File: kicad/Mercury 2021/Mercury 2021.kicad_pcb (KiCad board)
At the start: 2 copper layers, 57 parts, among them J1 Batt_Power, J10 3.3v rail, J11 Screw_Terminal_01x02, J12 Screw_Terminal_01x02, J13 Screw_Terminal_01x02, J14 Screw_Terminal_01x02, J15 Raspberry_Pi_2_3, J16 Sensors_Extra, J17 Arduino_Extra_Power, J18 Arduino_Extra_Comm, J19 Arduino_Extra_Digital, J2 Screw_Terminal_01x02, J20 Arduino_Extra_Analog, J21 MP_Extra_Analog, J22 Servos_Connector, J23 Pi_Extra_Comm, J24 Pi_Extra_GPIO, J25 Pi_Extra_GPIO, J26 Pi_Extra_Power, J27 Pi_Extra_GND, J28 Pi_Extra_GPIO, J29 Pi_Extra_GPIO, J3 Screw_Terminal_01x02, J30 Screw_Terminal_01x02, J31 Screw_Terminal_01x02, J32 Screw_Terminal_01x02, J33 Screw_Terminal_01x02, J34 Screw_Terminal_01x02, J35 Screw_Terminal_01x02, J36 GND rail 2, J37 GND rail 3, J38 USB_B, J39 USB_A, J4 Screw_Terminal_01x02, J5 Screw_Terminal_01x02, J6 Screw_Terminal_01x02, J7 5V rail, J8 GND Rail 1, J9 11v rail, U1 LM1084-5.0, U10 TCA9548APWR, U11 PCA9685, U12 PCA9685, U13 PCA9685, U2 Adafruit_VL53L0X, U3 Adafruit_VL53L0X, U4 Adafruit_VL53L0X, U5 Adafruit_VL53L0X, U6 Adafruit_VL53L0X, U7 Adafruit_VL53L0X, U8 Adafruit_VL53L0X, U9 Adafruit_VL53L0X

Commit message: Updated new board
- Did PCB traces
-- almost got away with just 2 copper layers, pi ruined it when there was only a bit to go. Probably possible but would take a lot of back and forth
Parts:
- removed C4: 10μf, Capacitor_THT:CP_Radial_D10.0mm_P2.50mm
- added U12A1: PCA9685, Connector_PinSocket_2.54mm:PinSocket_1x03_P2.54mm_Vertical, F.Cu at (83.6, 36.4)
- added U12B1: PCA9685, Connector_PinSocket_2.54mm:PinSocket_1x03_P2.54mm_Vertical, F.Cu at (80.0, 36.4)
- added U12C1: PCA9685, TerminalBlock:TerminalBlock_Altech_AK300-2_P5.00mm, F.Cu at (63.4, 87.9)
- added U12D1: PCA9685, Connector_PinSocket_2.54mm:PinSocket_1x03_P2.54mm_Vertical, F.Cu at (87.1, 36.4)
- added U12E1: PCA9685, Connector_PinSocket_2.54mm:PinSocket_1x03_P2.54mm_Vertical, F.Cu at (90.7, 36.4)
- J22: footprint Connector_PinSocket_2.54mm:PinSocket_2x03_P2.54mm_Vertical -> Connector_PinHeader_2.54mm:PinHeader_2x03_P2.54mm_Vertical
- U11, U13: footprint Connector_PinHeader_2.54mm:PinHeader_1x05_P2.54mm_Vertical -> Connector_JST:JST_EH_B5B-EH-A_1x05_P2.50mm_Vertical
- U12: footprint Connector_PinHeader_2.54mm:PinHeader_1x06_P2.54mm_Vertical -> Connector_PinSocket_2.54mm:PinSocket_1x06_P2.54mm_Vertical
- moved J8 248.1 mm to (48.4, 162.5)
- moved J7 246.5 mm to (48.5, 167.5)
- moved J9 231.0 mm to (37.5, 122.3), turned to 0 degrees
- moved J13 230.9 mm to (19.5, 112.1), turned to 90 degrees
- moved J34 221.2 mm to (19.2, 129.1), turned to 90 degrees
- moved J36 218.7 mm to (42.5, 122.5), turned to 0 degrees
- moved J11 213.4 mm to (19.5, 145.3), turned to 90 degrees
- moved J30 207.5 mm to (19.7, 163.1), turned to 90 degrees
- moved J32 206.0 mm to (18.9, 179.9), turned to 90 degrees
- moved J12 198.8 mm to (117.9, 182.9)
- moved J14 198.8 mm to (84.1, 182.9)
- moved J31 198.8 mm to (100.9, 182.9)
- moved J33 198.8 mm to (50.1, 182.9)
- moved J35 198.8 mm to (66.9, 182.9)
- moved C2 182.2 mm to (36.9, 162.1)
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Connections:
- net Arduino_3v3 renamed 3.3v_Rail
- net LM_VIN renamed 11.1v_Rail
- net SUB_D- renamed USB_D-
- C1 pad 2: LM_GND_MAIN -> GND_Rail
- C2 pad 1: MP_5v -> 5v_Rail
- C2 pad 2: LM_GND_MAIN -> GND_Rail
- C3 pad 2: Net-(C3-Pad2) -> GND_Rail
- J1 pad 1: LM_GND_MAIN -> GND_Rail
- J11 pad 1: LM_GND_MAIN -> GND_Rail
- J12 pad 1: MP_5v -> 5v_Rail
- J12 pad 2: LM_GND_MAIN -> GND_Rail
- J13 pad 1: LM_GND_MAIN -> GND_Rail
- J14 pad 1: MP_5v -> 5v_Rail
- J14 pad 2: LM_GND_MAIN -> GND_Rail
- J15 pad 1: /Motors/Pi_3v3 -> /Motors/Pi_3v3a
- J15 pad 17: /Motors/Pi_3v3 -> /Motors/Pi_3v3b
- J15 pad 2: MP_5v -> 5v_Rail
- J15 pad 20: LM_GND_MAIN -> /Motors/Pi_GNDa
- J15 pad 25: LM_GND_MAIN -> /Motors/Pi_GNDb
- J15 pad 30: LM_GND_MAIN -> /Motors/Pi_GNDc
- J15 pad 34: LM_GND_MAIN -> /Motors/Pi_GNDe
- J15 pad 39: Net-(J15-Pad39) -> GND_Rail
- J15 pad 4: MP_5v -> /Motors/Pi_5v_a
- J2 pad 2: LM_GND_MAIN -> GND_Rail
- J26 pad 1: MP_5v -> Net-(J26-Pad1)
- J26 pad 2: MP_5v -> /Motors/Pi_5v_a
- J26 pad 4: /Motors/Pi_3v3 -> /Motors/Pi_3v3a
- J26 pad 5: /Motors/Pi_3v3 -> /Motors/Pi_3v3b
- J27 pad 1: LM_GND_MAIN -> Net-(J27-Pad1)
- J27 pad 2: LM_GND_MAIN -> /Motors/Pi_GNDe
- J27 pad 3: LM_GND_MAIN -> /Motors/Pi_GNDc
- J27 pad 4: LM_GND_MAIN -> /Motors/Pi_GNDb
- J27 pad 5: LM_GND_MAIN -> /Motors/Pi_GNDa
- J3 pad 2: LM_GND_MAIN -> GND_Rail
- J30 pad 1: LM_GND_MAIN -> GND_Rail
- J31 pad 1: MP_5v -> 5v_Rail
- J31 pad 2: LM_GND_MAIN -> GND_Rail
- J32 pad 1: LM_GND_MAIN -> GND_Rail
- J33 pad 1: MP_5v -> 5v_Rail
- J33 pad 2: LM_GND_MAIN -> GND_Rail
- J34 pad 1: LM_GND_MAIN -> GND_Rail
- J35 pad 1: MP_5v -> 5v_Rail
- J35 pad 2: LM_GND_MAIN -> GND_Rail
- J36 pad 1: LM_GND_MAIN -> GND_Rail
- J36 pad 10: LM_GND_MAIN -> GND_Rail
- J36 pad 11: LM_GND_MAIN -> GND_Rail
- J36 pad 2: LM_GND_MAIN -> GND_Rail
- J36 pad 3: LM_GND_MAIN -> GND_Rail
- J36 pad 4: LM_GND_MAIN -> GND_Rail
- J36 pad 5: LM_GND_MAIN -> GND_Rail
- J36 pad 6: LM_GND_MAIN -> GND_Rail
- J36 pad 7: LM_GND_MAIN -> GND_Rail
- J36 pad 8: LM_GND_MAIN -> GND_Rail
- J36 pad 9: LM_GND_MAIN -> GND_Rail
- J37 pad 1: LM_GND_MAIN -> GND_Rail
- J37 pad 10: LM_GND_MAIN -> GND_Rail
- J37 pad 11: LM_GND_MAIN -> GND_Rail
- J37 pad 2: LM_GND_MAIN -> GND_Rail
- J37 pad 3: LM_GND_MAIN -> GND_Rail
- J37 pad 4: LM_GND_MAIN -> GND_Rail
- J37 pad 5: LM_GND_MAIN -> GND_Rail
- J37 pad 6: LM_GND_MAIN -> GND_Rail
- J37 pad 7: LM_GND_MAIN -> GND_Rail
- J37 pad 8: LM_GND_MAIN -> GND_Rail
- J37 pad 9: LM_GND_MAIN -> GND_Rail
- J4 pad 2: LM_GND_MAIN -> GND_Rail
- J5 pad 2: LM_GND_MAIN -> GND_Rail
- J6 pad 2: LM_GND_MAIN -> GND_Rail
- J7 pad 1: MP_5v -> 5v_Rail
- J7 pad 10: MP_5v -> 5v_Rail
- J7 pad 11: MP_5v -> 5v_Rail
- J7 pad 2: MP_5v -> 5v_Rail
- J7 pad 3: MP_5v -> 5v_Rail
- J7 pad 4: MP_5v -> 5v_Rail
- J7 pad 5: MP_5v -> 5v_Rail
- J7 pad 6: MP_5v -> 5v_Rail
- J7 pad 7: MP_5v -> 5v_Rail
- J7 pad 8: MP_5v -> 5v_Rail
- J7 pad 9: MP_5v -> 5v_Rail
- J8 pad 1: LM_GND_MAIN -> GND_Rail
- J8 pad 10: LM_GND_MAIN -> GND_Rail
- J8 pad 11: LM_GND_MAIN -> GND_Rail
- J8 pad 2: LM_GND_MAIN -> GND_Rail
- J8 pad 3: LM_GND_MAIN -> GND_Rail
- J8 pad 4: LM_GND_MAIN -> GND_Rail
- J8 pad 5: LM_GND_MAIN -> GND_Rail
- J8 pad 6: LM_GND_MAIN -> GND_Rail
- J8 pad 7: LM_GND_MAIN -> GND_Rail
- J8 pad 8: LM_GND_MAIN -> GND_Rail
- J8 pad 9: LM_GND_MAIN -> GND_Rail
- U1 pad 1: LM_GND_MAIN -> GND_Rail
- U1 pad 2: MP_5v -> 5v_Rail
- U10 pad 12: LM_GND_MAIN -> GND_Rail
- U10 pad 24: MP_5v -> 5v_Rail
- U12 pad 5: /Motors/Serco_VCC -> 5v_Rail
- U2 pad 1: MP_5v -> 5v_Rail
- U2 pad 2: LM_GND_MAIN -> GND_Rail
- U3 pad 1: MP_5v -> 5v_Rail
- U3 pad 2: LM_GND_MAIN -> GND_Rail
- U4 pad 1: MP_5v -> 5v_Rail
- U4 pad 2: LM_GND_MAIN -> GND_Rail
- U5 pad 1: MP_5v -> 5v_Rail
- U5 pad 2: LM_GND_MAIN -> GND_Rail
- U6 pad 1: MP_5v -> 5v_Rail
- U6 pad 2: LM_GND_MAIN -> GND_Rail
- U7 pad 1: MP_5v -> 5v_Rail
- U7 pad 2: LM_GND_MAIN -> GND_Rail
- U8 pad 1: /Sensors/VDD8 -> 5v_Rail
- U8 pad 2: /Sensors/GND8 -> GND_Rail
- U9 pad 1: MP_5v -> 5v_Rail
- U9 pad 2: LM_GND_MAIN -> GND_Rail
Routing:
- net GND_Rail: track 0.00 -> 995.7 mm, vias 0 -> 2
- net 5v_Rail: track 0.00 -> 683.0 mm
- net 3.3v_Rail: track 0.00 -> 286.9 mm
- net USB_GND: track 0.00 -> 269.0 mm
- net 11.1v_Rail: track 0.00 -> 164.5 mm
- net /Sensors/SDA: track 0.00 -> 153.1 mm
- net /Sensors/SCL: track 0.00 -> 126.1 mm
- net USB_D-: track 0.00 -> 126.1 mm
- net USB_D+: track 0.00 -> 125.5 mm
- net USB_VBUS: track 0.00 -> 123.9 mm
- net /Motors/RM_PWM2_GPIO12: track 0.00 -> 121.8 mm
- net USB_SHIELD: track 0.00 -> 121.5 mm
- net Net-(J22-Pad6): track 0.00 -> 97.8 mm, vias 0 -> 1
- net Net-(J22-Pad2): track 0.00 -> 97.4 mm, vias 0 -> 1
- net Net-(J22-Pad4): track 0.00 -> 97.1 mm, vias 0 -> 2
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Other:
- copper layers 2 -> 4
- board text added: "+"
- board text added: "-"
- board text added: "0"
- board text added: "00"
- board text added: "01"
- board text added: "04"
- board text added: "07"
- board text added: "08"
- board text added: "09"
- board text added: "1"
- board text added: "10"
- board text added: "11"
- board text added: "11v"
- board text added: "14"
- board text added: "15"
- board text added: "16"
- board text added: "17"
- board text added: "2"
- board text added: "22"
- board text added: "23"
- board text added: "24"
- board text added: "25"
- board text added: "26"
- board text added: "27"
- board text added: "3"
- board text added: "3.3v"
- board text added: "3v3"
- board text added: "4"
- board text added: "5"
- board text added: "5v"
- board text added: "6"
- board text added: "7"
- board text added: "A0"
- board text added: "A1"
- board text added: "A2"
- board text added: "A3"
- board text added: "A7"
- board text added: "A8"
- board text added: "AREF"
- board text added: "Battery"
- board text added: "D02"
- board text added: "D03"
- board text added: "D04"
- board text added: "D05"
- board text added: "D06"
- board text added: "D07"
- board text added: "D08"
- board text added: "D09"
- board text added: "D10"
- board text added: "GND"
- board text added: "GPIO"
- board text added: "Max Myzer made this PCB"
- board text added: "NC"
- board text added: "Pi_Extra Power"
- board text added: "Pi_Extra_GPIO"
- board text added: "RST"
- board text added: "Rst"
- board text added: "Rx"
- board text added: "SCL"
- board text added: "SDA"
- board text added: "Tx"
- board text added: "VIN"
- board text added: "XShut"

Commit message: New New board
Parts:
- removed C3: 10μf, Capacitor_THT:CP_Radial_D10.0mm_P2.50mm
- removed J11, J12, J34, J35, J6: Screw_Terminal_01x02, TerminalBlock:TerminalBlock_Altech_AK300-2_P5.00mm
- removed J22: Servos_Connector, Connector_PinHeader_2.54mm:PinHeader_2x03_P2.54mm_Vertical
- removed J23: Pi_Extra_Comm, Connector_PinSocket_2.54mm:PinSocket_1x02_P2.54mm_Vertical
- removed J24: Pi_Extra_GPIO, Connector_PinSocket_2.54mm:PinSocket_1x02_P2.54mm_Vertical
- removed J25: Pi_Extra_GPIO, Connector_PinSocket_2.54mm:PinSocket_1x06_P2.54mm_Vertical
- removed J26: Pi_Extra_Power, Connector_PinSocket_2.54mm:PinSocket_1x05_P2.54mm_Vertical
- removed J27: Pi_Extra_GND, Connector_PinSocket_2.54mm:PinSocket_1x05_P2.54mm_Vertical
- removed J28: Pi_Extra_GPIO, Connector_PinSocket_2.54mm:PinSocket_1x03_P2.54mm_Vertical
- removed J29: Pi_Extra_GPIO, Connector_PinSocket_2.54mm:PinSocket_1x05_P2.54mm_Vertical
- removed J38: USB_B, Connector_USB:USB_B_TE_5787834_Vertical
- removed J39: USB_A, Connector_USB:USB_A_Molex_105057_Vertical
- removed U12A1, U12B1, U12D1, U12E1: PCA9685, Connector_PinSocket_2.54mm:PinSocket_1x03_P2.54mm_Vertical
- J2, J3: value Screw_Terminal_01x02 -> Conn_01x20_Female; footprint TerminalBlock:TerminalBlock_Altech_AK300-2_P5.00mm -> Connector_PinSocket_2.54mm:PinSocket_1x20_P2.54mm_Vertical
- U11, U13: value PCA9685 -> MDD10A
- moved J37 235.9 mm to (39.2, 97.5), turned to 180 degrees
- moved J2 221.8 mm to (40.6, 108.5), turned to 90 degrees
- moved J3 196.8 mm to (40.6, 117.8), turned to 90 degrees
- moved J10 185.1 mm to (85.7, 70.7), turned to 180 degrees
- moved J14 168.7 mm to (27.5, 24.1), turned to 270 degrees
- moved J31 163.7 mm to (27.5, 36.6), turned to 270 degrees
- moved J17 158.1 mm to (43.2, 71.3), turned to 90 degrees
- moved J33 152.8 mm to (108.5, 41.7), turned to 90 degrees
- moved J5 149.6 mm to (108.8, 30.0), turned to 90 degrees
- moved A1 146.6 mm to (49.6, 89.9), turned to 90 degrees
- moved J18 143.3 mm to (52.1, 93.4), turned to 270 degrees
- moved C2 127.0 mm to (40.6, 35.1)
- moved U3 116.4 mm to (23.2, 82.1), turned to 180 degrees
- moved U6 114.3 mm to (31.3, 23.6), turned to 90 degrees
- moved J4 112.0 mm to (110.4, 90.7), turned to 90 degrees
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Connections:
- J15 pad 1: /Motors/Pi_3v3a -> /Motors/Pi01
- J15 pad 10: /Motors/Pi_GPIO15 -> /Motors/Pi10
- J15 pad 11: /Motors/Pi_GPIO17 -> /Motors/Pi11
- J15 pad 12: /Motors/RM_PWM1_GPIO18 -> /Motors/Pi12
- J15 pad 13: /Motors/Pi_GPIO27 -> /Motors/Pi13
- J15 pad 14: /Motors/Servo_CTL_GND -> /Motors/Pi14
- J15 pad 15: /Motors/Pi_GPIO22 -> /Motors/Pi15
- J15 pad 16: /Motors/Pi_GPIO23 -> /Motors/Pi16
- J15 pad 17: /Motors/Pi_3v3b -> /Motors/Pi17
- J15 pad 18: /Motors/Pi_GPIO24 -> /Motors/Pi18
- J15 pad 19: /Motors/Pi_GPIO10 -> /Motors/Pi19
- J15 pad 20: /Motors/Pi_GNDa -> /Motors/Pi20
- J15 pad 21: /Motors/Pi_GPIO09 -> /Motors/Pi21
- J15 pad 22: /Motors/Pi_GPIO25 -> /Motors/Pi22
- J15 pad 23: /Motors/Pi_GPIO11 -> /Motors/Pi23
- J15 pad 24: /Motors/Pi_GPIO08 -> /Motors/Pi24
- J15 pad 25: /Motors/Pi_GNDb -> /Motors/Pi25
- J15 pad 26: /Motors/Pi_GPIO07 -> /Motors/Pi26
- J15 pad 27: /Motors/Pi_GPIO00 -> /Motors/Pi27
- J15 pad 28: /Motors/Pi_GPIO01 -> /Motors/Pi28
- J15 pad 3: /Motors/Servo_SDA -> /Motors/Pi03
- J15 pad 30: /Motors/Pi_GNDc -> /Motors/Pi30
- J15 pad 32: /Motors/RM_PWM2_GPIO12 -> /Motors/Pi32
- J15 pad 34: /Motors/Pi_GNDe -> /Motors/Pi34
- J15 pad 36: /Motors/Pi_GPIO16 -> /Motors/Pi36
- J15 pad 37: /Motors/Pi_GPIO26 -> /Motors/Pi37
- J15 pad 38: /Motors/RM_DIR1_GPIO20 -> /Motors/Pi38
- J15 pad 4: /Motors/Pi_5v_a -> /Motors/Pi04
- J15 pad 40: /Motors/RM_DIR2_GPIO21 -> /Motors/Pi40
- J15 pad 5: /Motors/Servo_SCL -> /Motors/Pi05
- J15 pad 7: /Motors/Pi_GPIO04 -> /Motors/Pi07
- J15 pad 8: /Motors/Pi_GPIO14 -> /Motors/Pi08
- J15 pad 9: /Motors/RM_GND -> /Motors/Pi09
- J2 pad 1: 3.3v_Rail -> /Motors/Pi01
- J2 pad 2: GND_Rail -> /Motors/Pi03
- J20 pad 5: /Sensors/NC -> /Sensors/NCa
- J20 pad 6: /Sensors/NC -> /Sensors/NCb
- J3 pad 1: 3.3v_Rail -> 5v_Rail
- J3 pad 2: GND_Rail -> /Motors/Pi04
- J4 pad 1: 3.3v_Rail -> GND_Rail
- J4 pad 2: GND_Rail -> 11.1v_Rail
- J5 pad 1: 3.3v_Rail -> 5v_Rail
- U11 pad 1: /Motors/RM_DIR1_GPIO20 -> GND_Rail
- U11 pad 2: /Motors/RM_PWM1_GPIO18 -> 11.1v_Rail
- U11 pad 3: /Motors/RM_DIR2_GPIO21 -> /Motors/Pi40
- U11 pad 4: /Motors/RM_PWM2_GPIO12 -> /Motors/Pi32
- U11 pad 5: /Motors/RM_GND -> /Motors/Pi09
- U12 pad 1: /Motors/Servo_CTL_GND -> /Motors/Pi14
- U12 pad 3: /Motors/Servo_SCL -> /Motors/Pi05
- U12 pad 4: /Motors/Servo_SDA -> /Motors/Pi03
- U13 pad 2: /Motors/LM_PWM1_GPIO19 -> 11.1v_Rail
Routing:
- net GND_Rail: track 995.7 -> 142.2 mm, vias 2 -> 0
- net 5v_Rail: track 683.0 -> 3.16 mm
- net USB_GND: track 269.0 -> 0.00 mm
- net 3.3v_Rail: track 286.9 -> 30.7 mm
- net /Sensors/SDA: track 153.1 -> 15.2 mm
- net USB_D-: track 126.1 -> 0.00 mm
- net USB_D+: track 125.5 -> 0.00 mm
- net USB_VBUS: track 123.9 -> 0.00 mm
- net /Motors/RM_PWM2_GPIO12: track 121.8 -> 0.00 mm
- net USB_SHIELD: track 121.5 -> 0.00 mm
- net Net-(J22-Pad6): track 97.8 -> 0.00 mm, vias 1 -> 0
- net Net-(J22-Pad2): track 97.4 -> 0.00 mm, vias 1 -> 0
- net Net-(J22-Pad4): track 97.1 -> 0.00 mm, vias 2 -> 0
- net /Motors/RM_PWM1_GPIO18: track 96.0 -> 0.00 mm
- net /Motors/RM_DIR1_GPIO20: track 95.7 -> 0.00 mm
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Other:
- board outline added: 100 x 100 mm
- board text removed: "+"
- board text removed: "-"
- board text removed: "0"
- board text removed: "00"
- board text removed: "01"
- board text removed: "04"
- board text removed: "07"
- board text removed: "08"
- board text removed: "09"
- board text removed: "1"
- board text removed: "10"
- board text removed: "11"
- board text removed: "11v"
- board text removed: "14"
- board text removed: "15"
- board text removed: "16"
- board text removed: "17"
- board text removed: "2"
- board text removed: "22"
- board text removed: "23"
- board text removed: "24"
- board text removed: "25"
- board text removed: "26"
- board text removed: "27"
- board text removed: "3"
- board text removed: "3.3v"
- board text removed: "3v3"
- board text removed: "4"
- board text removed: "5"
- board text removed: "5v"
- board text removed: "6"
- board text removed: "7"
- board text removed: "A0"
- board text removed: "A1"
- board text removed: "A2"
- board text removed: "A3"
- board text removed: "A7"
- board text removed: "A8"
- board text removed: "AREF"
- board text removed: "Battery"
- board text removed: "D02"
- board text removed: "D03"
- board text removed: "D04"
- board text removed: "D05"
- board text removed: "D06"
- board text removed: "D07"
- board text removed: "D08"
- board text removed: "D09"
- board text removed: "D10"
- board text removed: "GND"
- board text removed: "GPIO"
- board text removed: "Max Myzer made this PCB"
- board text removed: "NC"
- board text removed: "Pi_Extra Power"
- board text removed: "Pi_Extra_GPIO"
- board text removed: "RST"
- board text removed: "Rst"
- board text removed: "Rx"
- board text removed: "SCL"
- board text removed: "SDA"
- board text removed: "Tx"
- board text removed: "VIN"
- board text removed: "XShut"

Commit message: Updated board
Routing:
- net 5v_Rail: track 3.16 -> 441.9 mm
- net GND_Rail: track 142.2 -> 540.6 mm

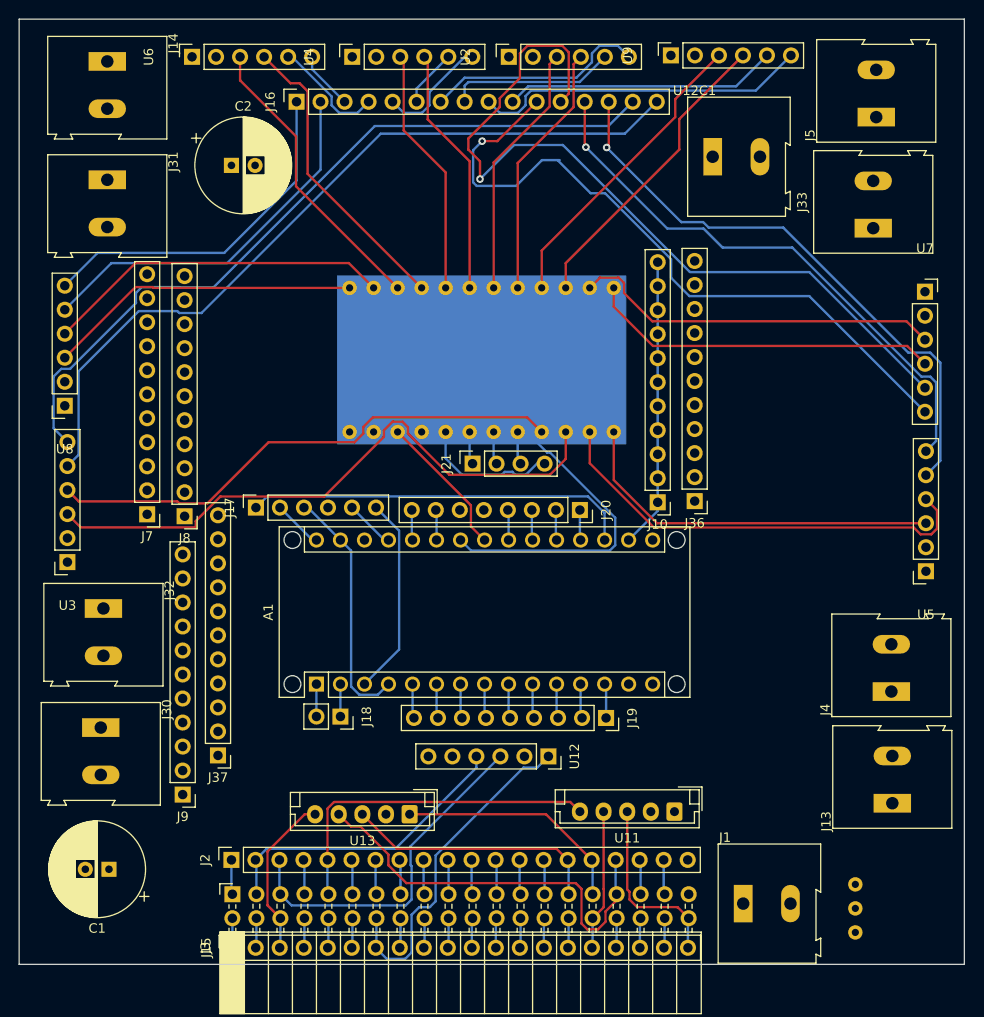
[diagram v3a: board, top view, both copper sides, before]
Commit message: Switched to 2 layers
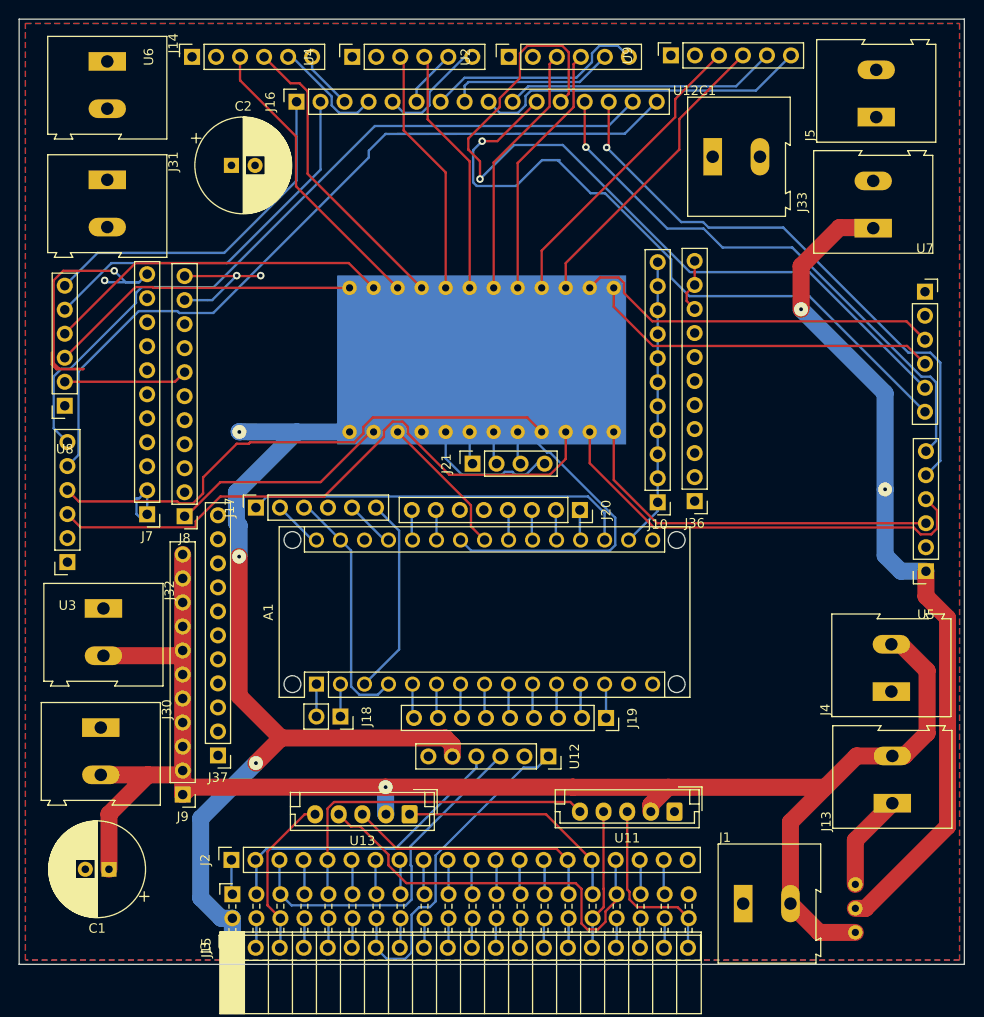
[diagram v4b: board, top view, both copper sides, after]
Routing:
- net GND_Rail: track 540.6 -> 67.4 mm, vias 0 -> 2
- net 5v_Rail: track 441.9 -> 224.3 mm, vias 0 -> 7
- net 11.1v_Rail: track 207.1 -> 175.7 mm, vias 0 -> 1
- net /Sensors/SDA0: track 55.5 -> 56.5 mm
- added copper zone on F.Cu, net 5v_Rail
- added copper zone on B.Cu, net GND_Rail
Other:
- copper layers 4 -> 2
